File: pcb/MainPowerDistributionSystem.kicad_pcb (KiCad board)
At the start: 4 copper layers, 66 x 60 mm, 85 parts, among them J2 PREC040DBAN-M71RC, U1 TPS22810DRV, U2 D24V7F5, U3 D24V7F3, U4 TMC2209-LA-T, U5 TMC2209-LA-T, U6 TMC2209-LA-T, U7 L4978, U8 L4978

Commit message: Renamed symbol and footprint `StackConnector` to `MainStackConnector`.
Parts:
- J1: footprint pcb:StackConnector -> pcb:MainStackConnector
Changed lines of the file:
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@@
 	(net 170 "Net-(U8-FB)")
 	(net 171 "Net-(JP8-B)")
-	(footprint "pcb:StackConnector"
+	(footprint "pcb:MainStackConnector"
 		(locked yes)
 		(layer "F.Cu")

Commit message: Removed stepper motor drivers from `MainPowerDistributionSystem`.
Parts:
- removed C1, C10, C14, C15, C17, C18, C2, C22, C23, C6, C7, C9: 100n, Capacitor_SMD:C_1206_3216Metric_Pad1.33x1.80mm_HandSolder
- removed C11, C13, C19, C21, C3, C5: 10n, Capacitor_SMD:C_1206_3216Metric_Pad1.33x1.80mm_HandSolder
- removed C12, C20, C4: 2u2, Capacitor_SMD:C_1206_3216Metric_Pad1.33x1.80mm_HandSolder
- removed C16, C24, C8: 865080343009, Capacitor_SMD:CP_Elec_6.3x5.4
- removed D1, D2, D3: YELLOW, LED_SMD:LED_1206_3216Metric_Pad1.42x1.75mm_HandSolder
- removed JP1: Jumper_2_Bridged, Jumper:SolderJumper-2_P1.3mm_Open_RoundedPad1.0x1.5mm
- removed JP2, JP3, JP4, JP5, JP6, JP7, JP8: SolderJumper_2_Open, Jumper:SolderJumper-2_P1.3mm_Open_RoundedPad1.0x1.5mm
- removed R1, R2: 1k, Resistor_SMD:R_1206_3216Metric_Pad1.30x1.75mm_HandSolder
- removed R10, R4, R7: 2k, Resistor_SMD:R_1206_3216Metric_Pad1.30x1.75mm_HandSolder
- removed R11, R12, R5, R6, R8, R9: RL1206FR-070R05L, Resistor_SMD:R_1206_3216Metric_Pad1.30x1.75mm_HandSolder
- removed R3: 20k, Resistor_SMD:R_1206_3216Metric_Pad1.30x1.75mm_HandSolder
- removed TP1, TP2, TP3, TP4, TP5: TestPoint, TestPoint:TestPoint_Pad_1.0x1.0mm
- removed U1: TPS22810DRV, Package_SON:WSON-6-1EP_2x2mm_P0.65mm_EP1x1.6mm
- removed U4, U5, U6: TMC2209-LA-T, Package_DFN_QFN:VQFN-28-1EP_5x5mm_P0.5mm_EP3.7x3.7mm_ThermalVias
- moved U2 6.52 mm to (133.7, 115.5)
- moved U3 6.52 mm to (143.0, 115.5)
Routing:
- net +MOTOR: track 95.4 -> 0.00 mm, vias 18 -> 0
- net GND: track 37.3 -> 7.00 mm, vias 39 -> 12
- net MOTOR_UART_RX: track 15.1 -> 0.00 mm
- net /Stepper Motor Driver - X/SPREAD: track 14.8 -> 0.00 mm
- net Net-(U5-CPO): track 9.29 -> 0.00 mm, vias 1 -> 0
- net Net-(U6-CPO): track 9.29 -> 0.00 mm, vias 1 -> 0
- net Net-(U4-CPO): track 9.29 -> 0.00 mm, vias 1 -> 0
- net MOTOR_DRIVER_B2_Y: track 8.83 -> 0.00 mm
- net MOTOR_DRIVER_B2_X: track 8.83 -> 0.00 mm
- net MOTOR_DRIVER_B2_Z: track 8.83 -> 0.00 mm
- net /Stepper Motor Driver - X/DISABLE: track 8.19 -> 0.00 mm
- net Net-(JP4-B): track 8.00 -> 0.00 mm, vias 2 -> 0
- net Net-(JP6-B): track 8.00 -> 0.00 mm, vias 2 -> 0
- net Net-(JP8-B): track 8.00 -> 0.00 mm, vias 2 -> 0
- net Net-(JP3-B): track 7.91 -> 0.00 mm, vias 2 -> 0
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
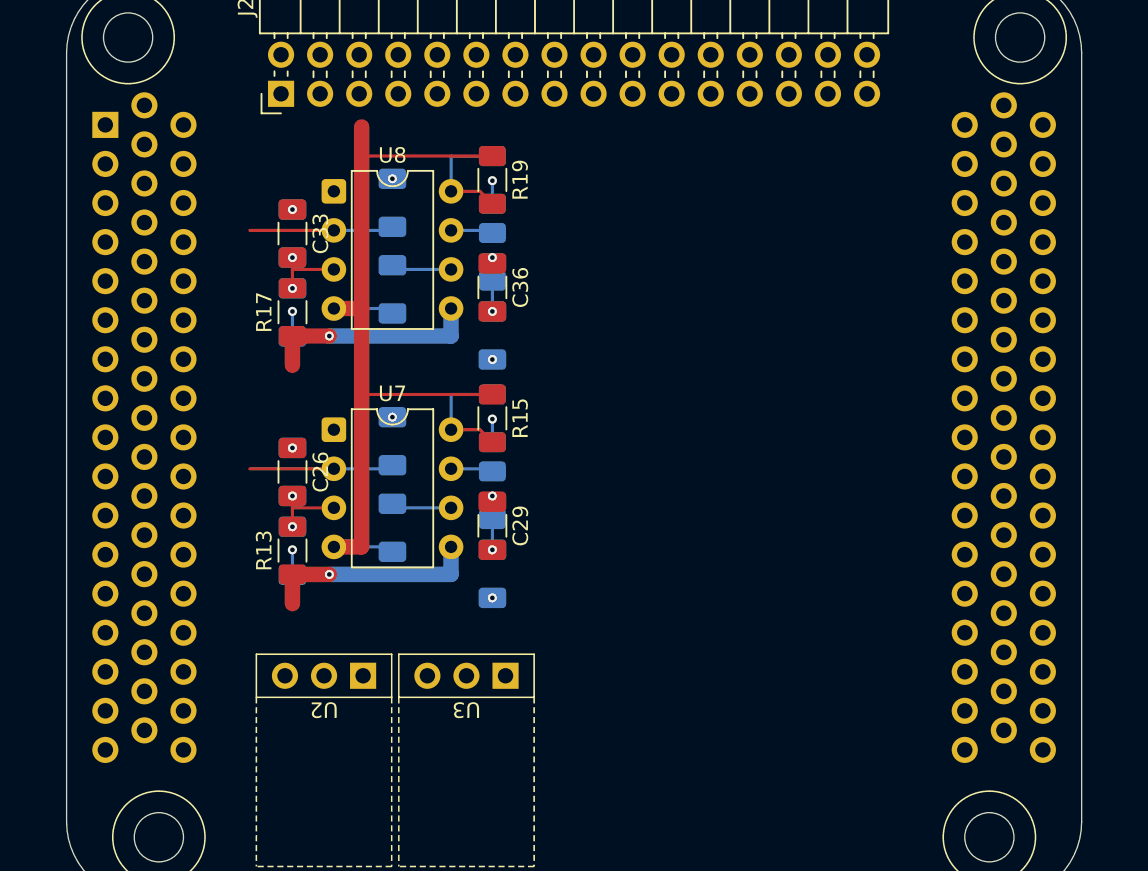
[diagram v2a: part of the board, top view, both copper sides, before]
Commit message: Updated main stack-up connector design to go from 6 1x17 headers to only 4 1x17 headers.
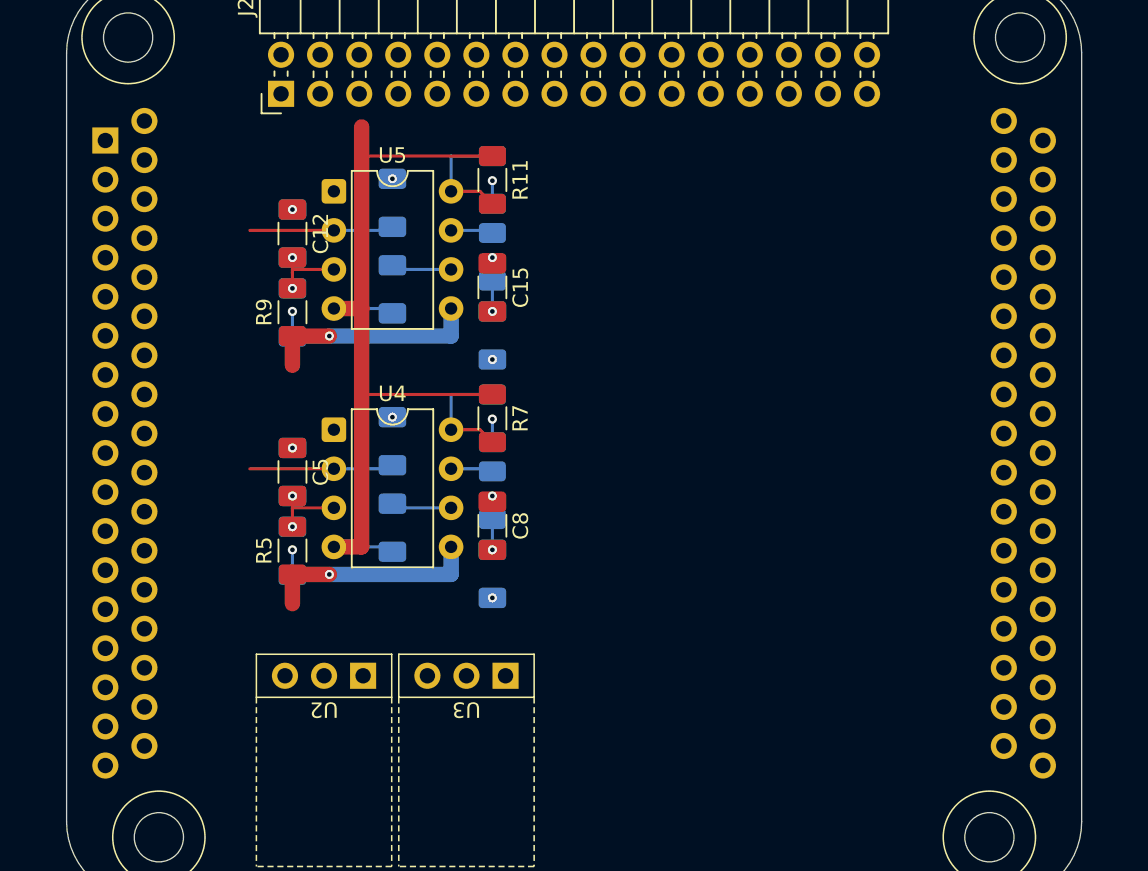
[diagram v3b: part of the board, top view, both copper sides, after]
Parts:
- renumbered C31 to C10, C32 to C11, C33 to C12, C34 to C13, C35 to C14, C36 to C15, C37 to C16, C38 to C17, C25 to C4, C26 to C5, C27 to C6, C28 to C7, C29 to C8, C30 to C9, R18 to R10, R19 to R11, R20 to R12, R13 to R5, R14 to R6, R15 to R7, R16 to R8, R17 to R9, U7 to U4, U8 to U5
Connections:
- J1 pad 12: MOTOR_UART_TX -> unconnected-(J1-uart_tx_A-Pad12)
- J1 pad 13: MOTOR_UART_RX -> unconnected-(J1-uart_rx_A-Pad13)
- J1 pad 41: MOTOR_STEP_X -> unconnected-(J1-general_purpose_E-Pad41)
- J1 pad 42: MOTOR_DIR_X -> unconnected-(J1-general_purpose_F-Pad42)
- J1 pad 43: MOTOR_STEP_Y -> unconnected-(J1-general_purpose_G-Pad43)
- J1 pad 44: MOTOR_DIR_Y -> unconnected-(J1-general_purpose_H-Pad44)
- J1 pad 45: MOTOR_STEP_Z -> unconnected-(J1-general_purpose_I-Pad45)
- J1 pad 46: MOTOR_DIR_Z -> unconnected-(J1-general_purpose_J-Pad46)
- J1 pad 47: MOTOR_DISABLE -> unconnected-(J1-general_purpose_K-Pad47)

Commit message: Cleaned up and prepared `MainPowerDistributionSystem`.
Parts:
- removed C10, C14, C17, C7: 100n, Capacitor_SMD:C_1206_3216Metric_Pad1.33x1.80mm_HandSolder
- removed C11, C12, C13, C4, C5, C6: 1n, Capacitor_SMD:C_1206_3216Metric_Pad1.33x1.80mm_HandSolder
- removed C15, C16, C8, C9: 10n, Capacitor_SMD:C_1206_3216Metric_Pad1.33x1.80mm_HandSolder
- removed R10, R6: 9k1, Resistor_SMD:R_1206_3216Metric_Pad1.30x1.75mm_HandSolder
- removed R11, R12, R7, R8: 0, Resistor_SMD:R_1206_3216Metric_Pad1.30x1.75mm_HandSolder
- removed R5, R9: 20k, Resistor_SMD:R_1206_3216Metric_Pad1.30x1.75mm_HandSolder
- removed U2: D24V7F5, pcb:D24V7Fx
- removed U3: D24V7F3, pcb:D24V7Fx
- removed U4, U5: L4978, Package_DIP:DIP-8_W7.62mm
- J2: footprint Connector_PinHeader_2.54mm:PinHeader_2x16_P2.54mm_Horizontal -> pcb:PinHeader_2x16_P2.54mm_Horizontal_SmallSilkscreen
- moved J2 1.02 mm to (130.9, 76.6)
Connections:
- net MOTOR_DRIVER_A1_Z renamed +TE-X
- J1 pad 48: unconnected-(J1-general_purpose_L-Pad48) -> LOGIC_GSE_1
- J1 pad 49: unconnected-(J1-general_purpose_M-Pad49) -> LOGIC_TIMER_EVENT_1
- J1 pad 50: unconnected-(J1-general_purpose_N-Pad50) -> LOGIC_TIMER_EVENT_X
- J2 pad 1: MOTOR_DRIVER_A1_X -> +GSE-1
- J2 pad 10: MOTOR_DRIVER_B1_Z -> unconnected-(J2-Pin_10-Pad10)
- J2 pad 11: MOTOR_DRIVER_A2_Z -> GND
- J2 pad 12: MOTOR_DRIVER_B2_Z -> unconnected-(J2-Pin_12-Pad12)
- J2 pad 13: +GSE-1 -> +3.3V
- J2 pad 14: +TE-RA -> unconnected-(J2-Pin_14-Pad14)
- J2 pad 16: GND -> unconnected-(J2-Pin_16-Pad16)
- J2 pad 17: +GSE-2 -> +3.3V
- J2 pad 18: +TE-RB -> unconnected-(J2-Pin_18-Pad18)
- J2 pad 2: MOTOR_DRIVER_B1_X -> BURNWIRE_VOLTAGE
- J2 pad 20: GND -> unconnected-(J2-Pin_20-Pad20)
- J2 pad 21: +TE-1 -> +3.3V
- J2 pad 22: +BATT-1 -> unconnected-(J2-Pin_22-Pad22)
- J2 pad 24: GND -> unconnected-(J2-Pin_24-Pad24)
- J2 pad 25: +TE-2 -> +3.3V
- J2 pad 26: +BATT-2 -> unconnected-(J2-Pin_26-Pad26)
- J2 pad 28: GND -> unconnected-(J2-Pin_28-Pad28)
- J2 pad 29: +TE-3 -> unconnected-(J2-Pin_29-Pad29)
- J2 pad 3: MOTOR_DRIVER_A2_X -> GND
- J2 pad 30: BURNWIRE_VOLTAGE -> unconnected-(J2-Pin_30-Pad30)
- J2 pad 31: GND -> unconnected-(J2-Pin_31-Pad31)
- J2 pad 32: GND -> unconnected-(J2-Pin_32-Pad32)
- J2 pad 4: MOTOR_DRIVER_B2_X -> GND
- J2 pad 5: MOTOR_DRIVER_A1_Y -> +TE-1
- J2 pad 6: MOTOR_DRIVER_B1_Y -> BURNWIRE_VOLTAGE
- J2 pad 7: MOTOR_DRIVER_A2_Y -> GND
- J2 pad 8: MOTOR_DRIVER_B2_Y -> GND
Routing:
- net BURNWIRE_VOLTAGE: track 55.8 -> 0.00 mm
- net +BURNWIRE: track 28.0 -> 0.00 mm, vias 2 -> 0
- net BURNWIRE_ENABLE: track 18.7 -> 0.00 mm
- net Net-(U5-FB): track 8.00 -> 0.00 mm
- net Net-(U4-FB): track 8.00 -> 0.00 mm
- net Net-(U5-OSC): track 4.92 -> 0.00 mm, vias 2 -> 0
- net Net-(U4-OSC): track 4.92 -> 0.00 mm, vias 2 -> 0
- net Net-(U5-BOOT): track 3.93 -> 0.00 mm
- net Net-(U4-BOOT): track 3.93 -> 0.00 mm
- net Net-(U5-COMP): track 2.76 -> 0.00 mm
- net Net-(U4-COMP): track 2.76 -> 0.00 mm
- net Net-(C8-Pad2): track 2.00 -> 0.00 mm, vias 1 -> 0
- net Net-(C15-Pad2): track 2.00 -> 0.00 mm, vias 1 -> 0
- net GND: track 7.00 -> 6.13 mm, vias 12 -> 0
- added copper zone on F.Cu, net +3.3V
- removed copper zone on In2.Cu, net +3.3V
- removed copper zone on F.Cu, net GND
- removed copper zone on In1.Cu, net GND
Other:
- copper layers 4 -> 2

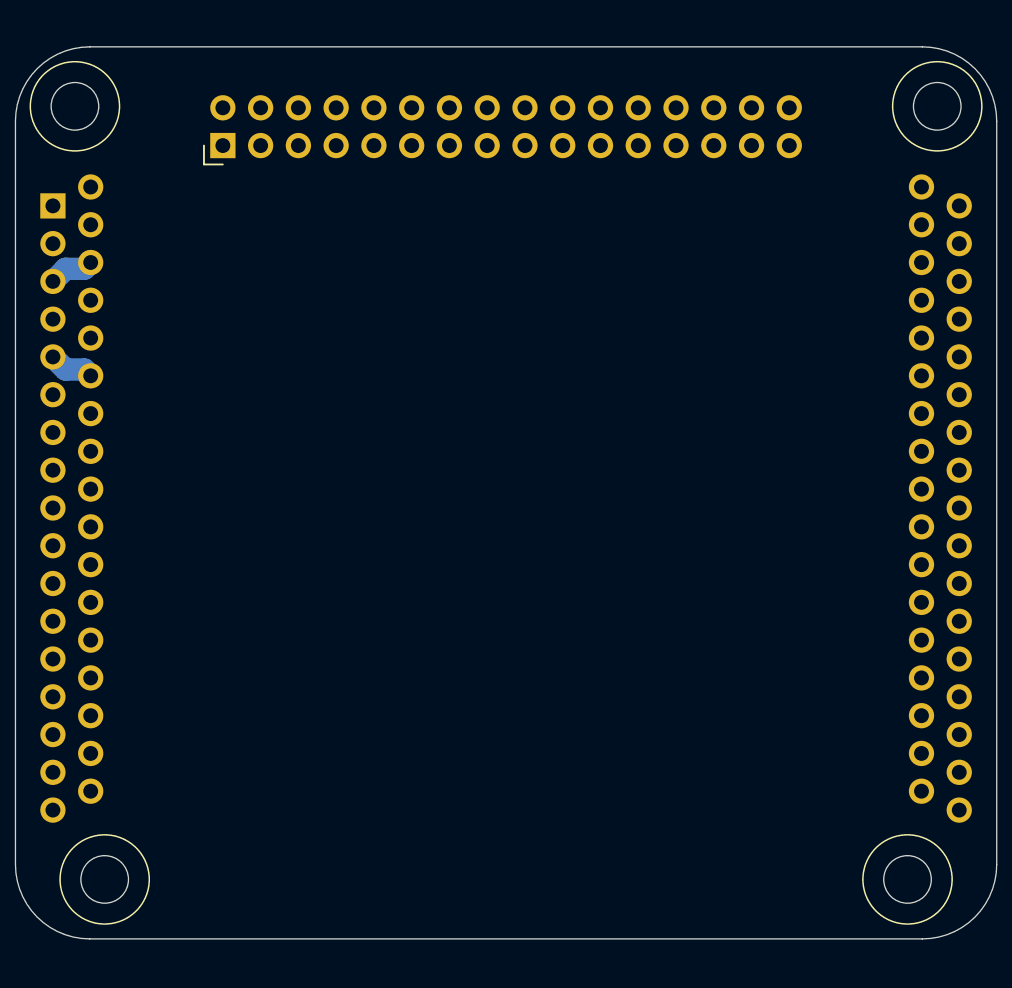
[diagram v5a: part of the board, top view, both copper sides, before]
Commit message: Added burn wire timer to schematic and routed PCB
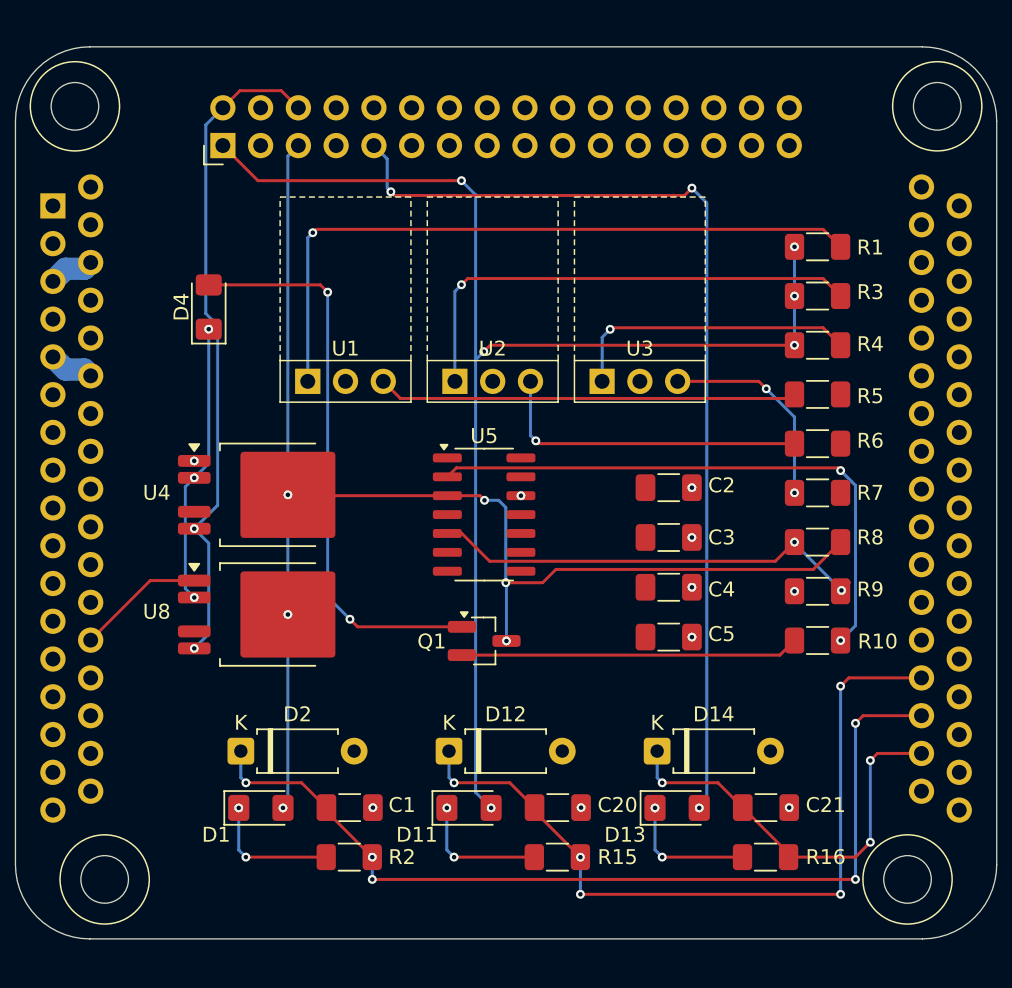
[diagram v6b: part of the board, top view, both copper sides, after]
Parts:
- added C1: 1u, Capacitor_SMD:C_1206_3216Metric_Pad1.33x1.80mm_HandSolder, F.Cu at (139.5, 121.2)
- added C2: 1u, Capacitor_SMD:C_1206_3216Metric_Pad1.33x1.80mm_HandSolder, F.Cu at (160.9, 99.7)
- added C20: 1u, Capacitor_SMD:C_1206_3216Metric_Pad1.33x1.80mm_HandSolder, F.Cu at (153.5, 121.2)
- added C21: 1u, Capacitor_SMD:C_1206_3216Metric_Pad1.33x1.80mm_HandSolder, F.Cu at (167.5, 121.2)
- added C3: 1u, Capacitor_SMD:C_1206_3216Metric_Pad1.33x1.80mm_HandSolder, F.Cu at (160.9, 103.0)
- added C4: 1u, Capacitor_SMD:C_1206_3216Metric_Pad1.33x1.80mm_HandSolder, F.Cu at (160.9, 106.3)
- added C5: 1u, Capacitor_SMD:C_1206_3216Metric_Pad1.33x1.80mm_HandSolder, F.Cu at (160.9, 109.7)
- added D1: WHITE, LED_SMD:LED_1206_3216Metric_Pad1.42x1.75mm_HandSolder, F.Cu at (133.5, 121.2)
- added D11: WHITE, LED_SMD:LED_1206_3216Metric_Pad1.42x1.75mm_HandSolder, F.Cu at (147.5, 121.2)
- added D12: 1N4727A, Diode_THT:D_A-405_P7.62mm_Horizontal, F.Cu at (146.2, 117.4)
- added D13: WHITE, LED_SMD:LED_1206_3216Metric_Pad1.42x1.75mm_HandSolder, F.Cu at (161.5, 121.2)
- added D14: 1N4727A, Diode_THT:D_A-405_P7.62mm_Horizontal, F.Cu at (160.2, 117.4)
- added D2: 1N4727A, Diode_THT:D_A-405_P7.62mm_Horizontal, F.Cu at (132.2, 117.4)
- added D4: RED, LED_SMD:LED_1206_3216Metric_Pad1.42x1.75mm_HandSolder, F.Cu at (130.0, 87.5)
- added Q1: S8050, Package_TO_SOT_SMD:SOT-23_Handsoldering, F.Cu at (148.5, 110.0)
- added R1: 0, Resistor_SMD:R_1206_3216Metric_Pad1.30x1.75mm_HandSolder, F.Cu at (170.9, 83.5)
- added R10: 10k, Resistor_SMD:R_1206_3216Metric_Pad1.30x1.75mm_HandSolder, F.Cu at (170.9, 109.9)
- added R15: 3k, Resistor_SMD:R_1206_3216Metric_Pad1.30x1.75mm_HandSolder, F.Cu at (153.4, 124.5)
- added R16: 3k, Resistor_SMD:R_1206_3216Metric_Pad1.30x1.75mm_HandSolder, F.Cu at (167.4, 124.5)
- added R2: 3k, Resistor_SMD:R_1206_3216Metric_Pad1.30x1.75mm_HandSolder, F.Cu at (139.4, 124.5)
- added R3: 0, Resistor_SMD:R_1206_3216Metric_Pad1.30x1.75mm_HandSolder, F.Cu at (170.9, 86.8)
- added R4: 0, Resistor_SMD:R_1206_3216Metric_Pad1.30x1.75mm_HandSolder, F.Cu at (170.9, 90.1)
- added R5: 0, Resistor_SMD:R_1206_3216Metric_Pad1.30x1.75mm_HandSolder, F.Cu at (170.9, 93.4)
- added R6: 0, Resistor_SMD:R_1206_3216Metric_Pad1.30x1.75mm_HandSolder, F.Cu at (170.9, 96.7)
- added R7: 0, Resistor_SMD:R_1206_3216Metric_Pad1.30x1.75mm_HandSolder, F.Cu at (170.9, 100.0)
- added R8: 910k, Resistor_SMD:R_1206_3216Metric_Pad1.30x1.75mm_HandSolder, F.Cu at (170.9, 103.3)
- added R9: 360k, Resistor_SMD:R_1206_3216Metric_Pad1.30x1.75mm_HandSolder, F.Cu at (170.9, 106.6)
- added U1: D24V7F3, pcb:D24V7Fx, F.Cu at (139.2, 92.5)
- added U2: D24V7F3, pcb:D24V7Fx, F.Cu at (149.1, 92.5)
- added U3: D24V7F3, pcb:D24V7Fx, F.Cu at (159.0, 92.5)
- added U4: BTS462TATMA1, Package_TO_SOT_SMD:TO-252-4, F.Cu at (134.1, 100.1)
- added U5: LM339, Package_SO:SOIC-14_3.9x8.7mm_P1.27mm, F.Cu at (148.5, 101.5)
- added U8: BTS462TATMA1, Package_TO_SOT_SMD:TO-252-4, F.Cu at (134.1, 108.2)
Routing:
- net +TE-1: track 0.00 -> 92.6 mm, vias 0 -> 6
- net +GSE-1: track 0.00 -> 88.5 mm, vias 0 -> 6
- net +TE-X: track 0.00 -> 66.5 mm, vias 0 -> 3
- net LOGIC_TIMER_EVENT_1: track 0.00 -> 62.1 mm, vias 0 -> 5
- net LOGIC_GSE_1: track 0.00 -> 52.7 mm, vias 0 -> 5
- net Net-(R1-Pad2): track 0.00 -> 46.2 mm, vias 0 -> 1
- net BURNWIRE_VOLTAGE: track 0.00 -> 44.7 mm, vias 0 -> 2
- net Net-(R10-Pad2): track 0.00 -> 39.0 mm, vias 0 -> 2
- net Net-(D4-A): track 0.00 -> 38.6 mm, vias 0 -> 2
- net Net-(R3-Pad2): track 0.00 -> 32.8 mm, vias 0 -> 1
- net Net-(U5A-+): track 0.00 -> 30.3 mm, vias 0 -> 2
- net Net-(R5-Pad1): track 0.00 -> 28.2 mm
- net LOGIC_TIMER_EVENT_X: track 0.00 -> 28.0 mm, vias 0 -> 3
- net Net-(Q1-B): track 0.00 -> 22.8 mm
- net Net-(R6-Pad1): track 0.00 -> 21.6 mm, vias 0 -> 1
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
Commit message: Fixed burn-wire enable circuit on schematic and PCB for MPDS
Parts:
- removed R10: 10k, Resistor_SMD:R_1206_3216Metric_Pad1.30x1.75mm_HandSolder
- added C6: 22u, Capacitor_SMD:C_1206_3216Metric_Pad1.33x1.80mm_HandSolder, F.Cu at (171.0, 110.5)
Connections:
- D4 pad 1: Net-(D4-K) -> BURNWIRE_VOLTAGE
- U4 pad 2: Net-(D4-K) -> Net-(U4-IN)
- U4 pad 5: BURNWIRE_VOLTAGE -> Net-(D4-A)
- U5 pad 1: (no net) -> unconnected-(U5-Pad1)
- U5 pad 10: (no net) -> unconnected-(U5C---Pad10)
- U5 pad 11: (no net) -> unconnected-(U5C-+-Pad11)
- U5 pad 13: (no net) -> unconnected-(U5-Pad13)
- U5 pad 14: (no net) -> unconnected-(U5-Pad14)
- U5 pad 2: Net-(R10-Pad2) -> Net-(U4-IN)
- U5 pad 6: (no net) -> unconnected-(U5B---Pad6)
- U5 pad 7: (no net) -> unconnected-(U5B-+-Pad7)
- U5 pad 8: (no net) -> unconnected-(U5D---Pad8)
- U5 pad 9: (no net) -> unconnected-(U5D-+-Pad9)
- U8 pad 2: Net-(D4-K) -> Net-(U4-IN)
- U8 pad 5: BURNWIRE_VOLTAGE -> Net-(D4-A)
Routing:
- net Net-(R10-Pad2): track 39.0 -> 0.00 mm, vias 2 -> 0
- net Net-(U4-IN): track 0.00 -> 27.3 mm, vias 0 -> 2
- net +TE-1: track 92.6 -> 116.7 mm, vias 6 -> 16
- net BURNWIRE_VOLTAGE: track 44.7 -> 21.5 mm, vias 2 -> 1
- net Net-(Q1-B): track 22.8 -> 0.00 mm
- net Net-(D4-K): track 19.0 -> 0.00 mm, vias 3 -> 0
- net Net-(D4-A): track 38.6 -> 55.5 mm, vias 2 -> 6
- net Net-(U5A-+): track 30.3 -> 35.5 mm, vias 2 -> 3
- net +3.3V: track 0.00 -> 4.00 mm, vias 0 -> 2
- net GND: vias 10 -> 11
